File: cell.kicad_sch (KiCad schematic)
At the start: 31 parts, among them K4 V23105A5001A201, Q12 IRLML0030, Q13 IRLML0030, SW8 SW_SPST, SW9 SW_SPST, U6 LMV324

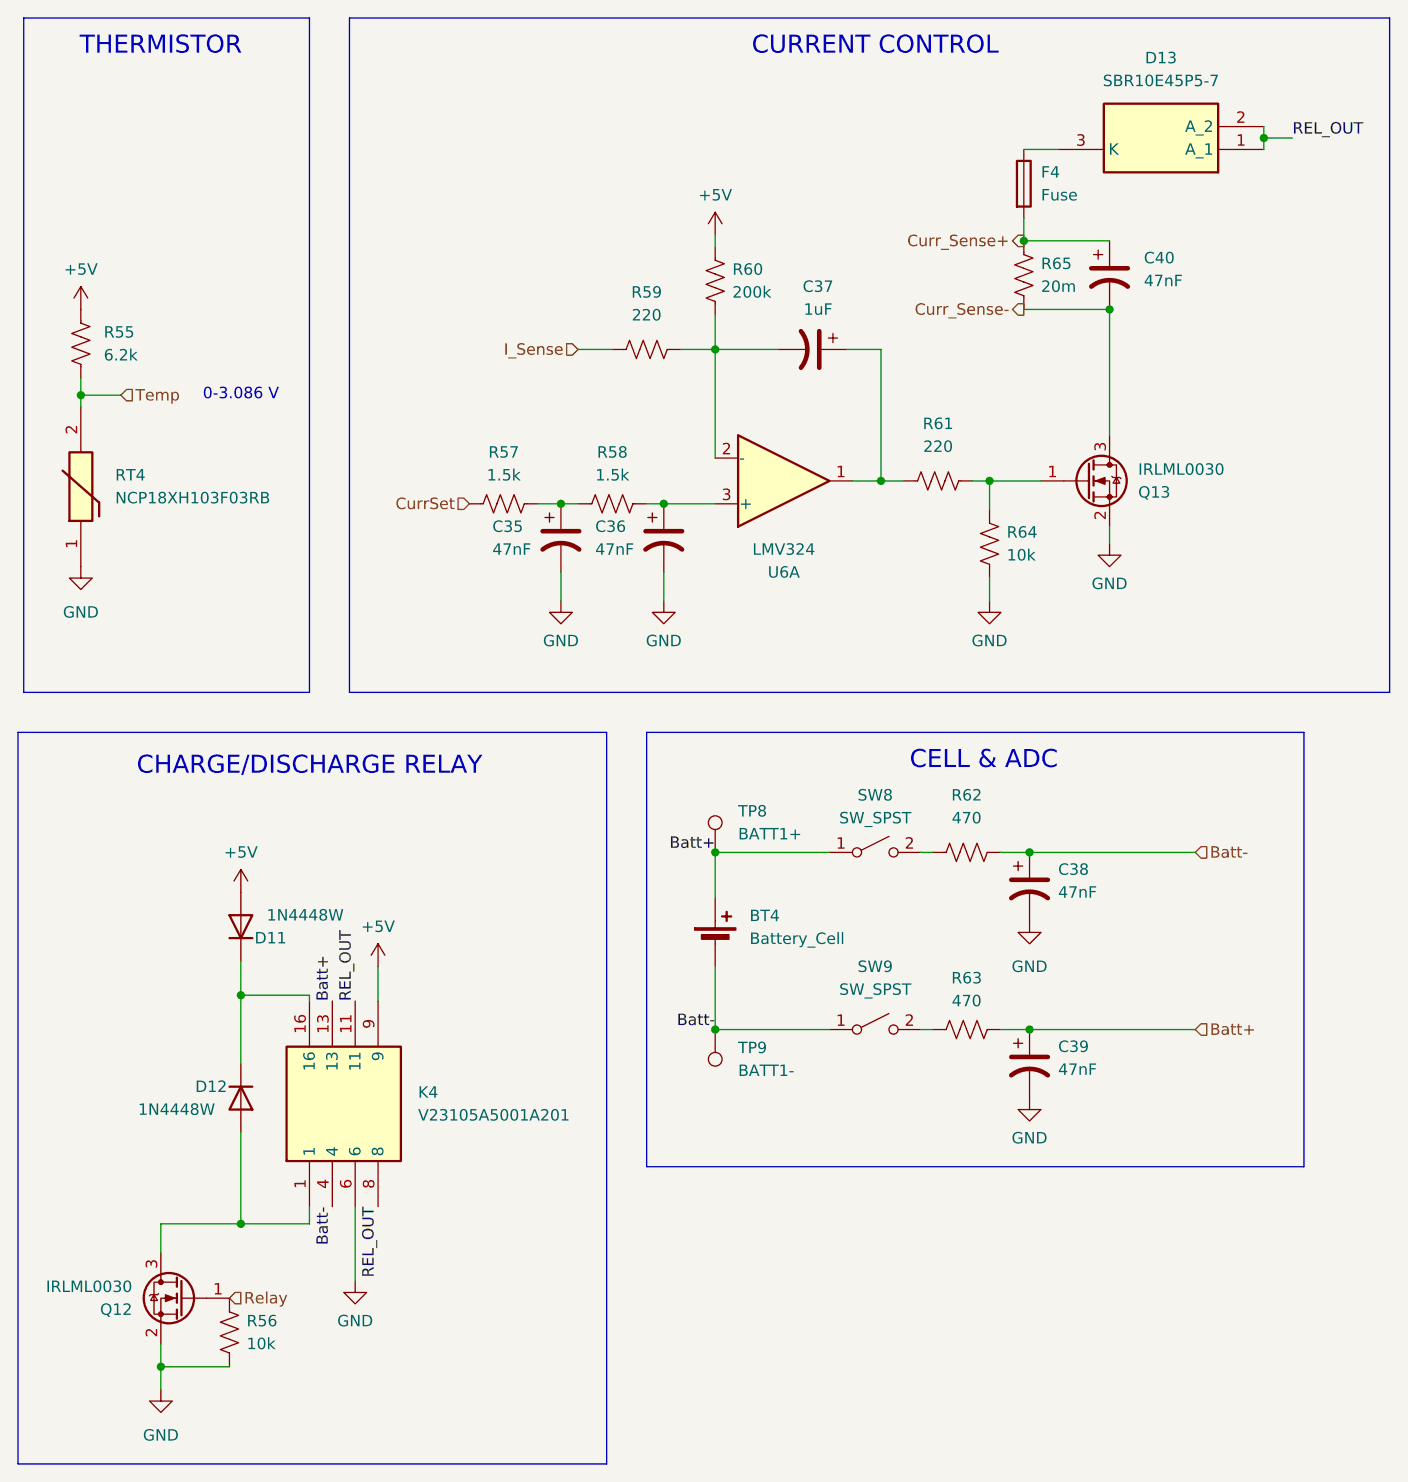
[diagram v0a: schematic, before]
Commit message: added logic level translator
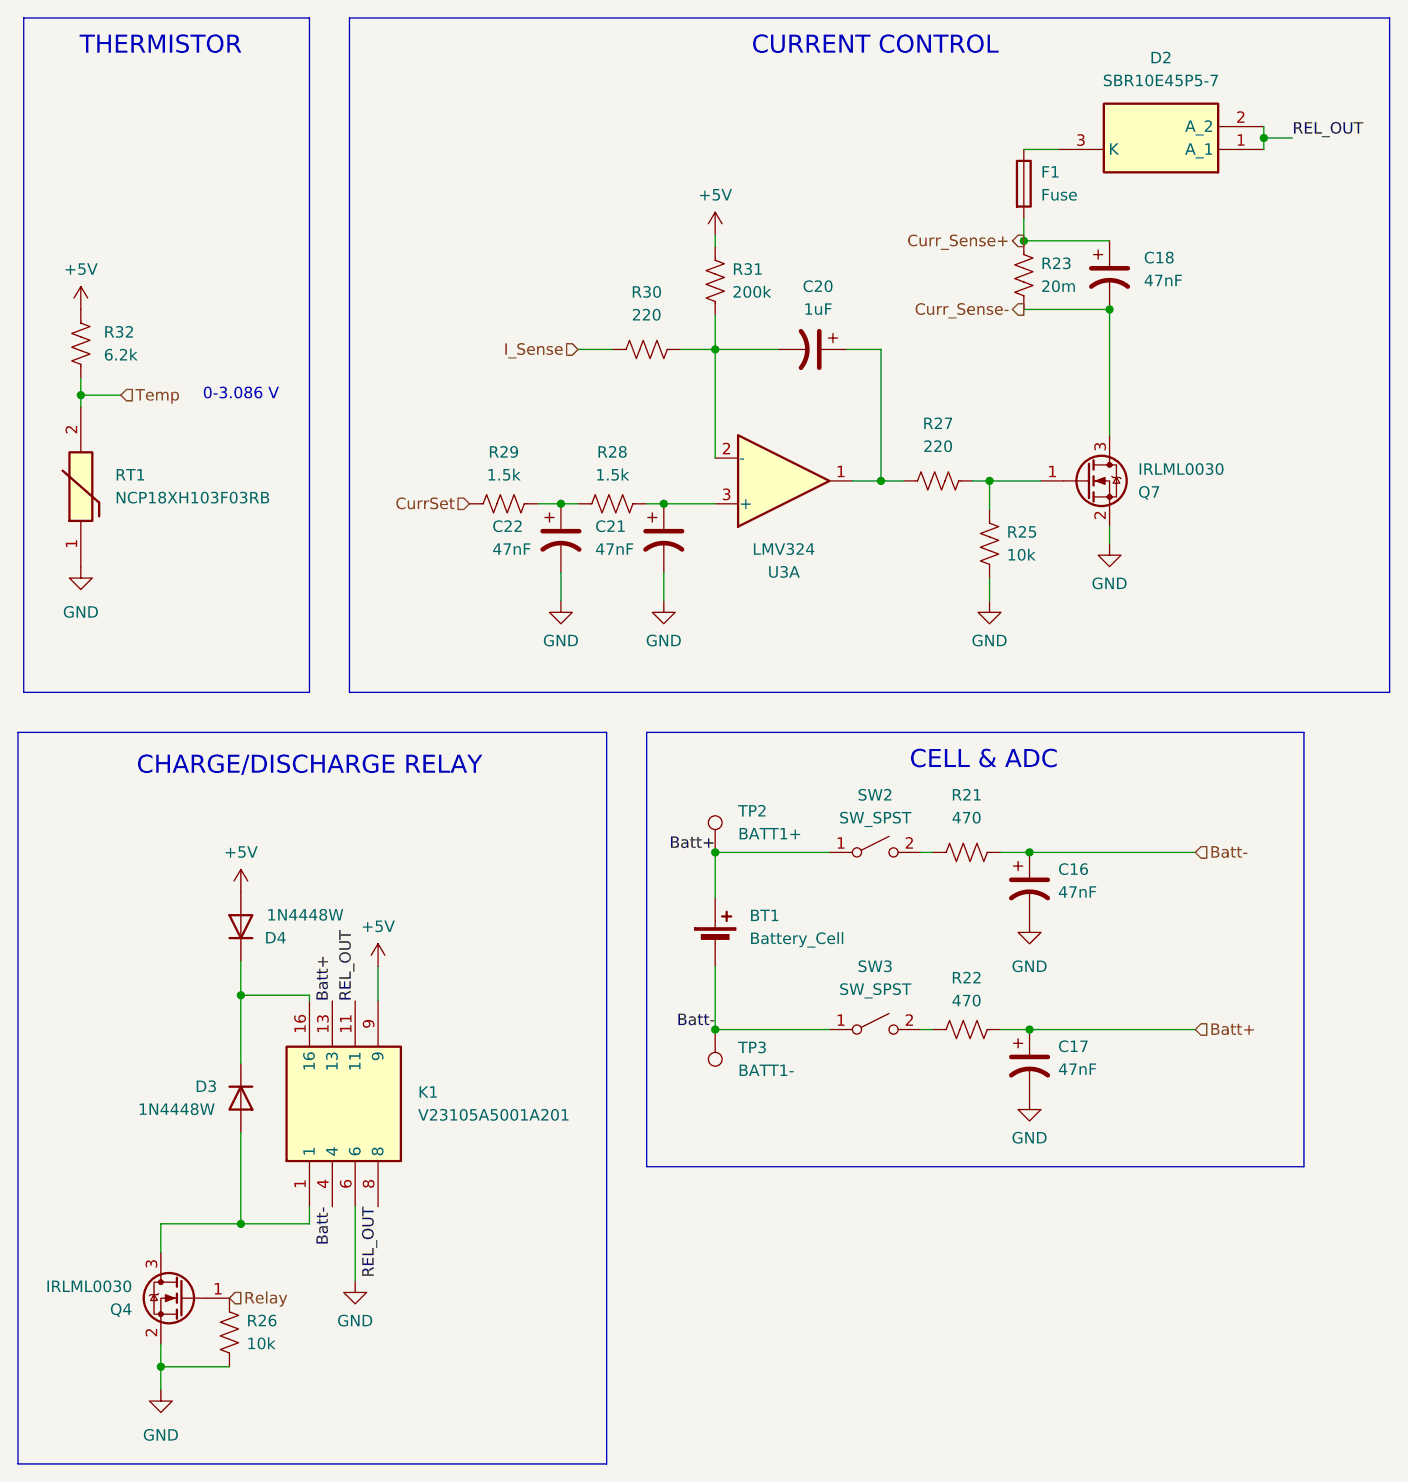
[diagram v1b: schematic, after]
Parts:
- renumbered BT4 to BT1, C38 to C16, C39 to C17, C40 to C18, C37 to C20, C36 to C21, C35 to C22, D13 to D2, D12 to D3, D11 to D4, F4 to F1, K4 to K1, Q12 to Q4, Q13 to Q7, R62 to R21, R63 to R22, R65 to R23, R64 to R25, R56 to R26, R61 to R27, R58 to R28, R57 to R29, R59 to R30, R60 to R31, R55 to R32, RT4 to RT1, SW8 to SW2, SW9 to SW3, TP8 to TP2, TP9 to TP3, U6 to U3
